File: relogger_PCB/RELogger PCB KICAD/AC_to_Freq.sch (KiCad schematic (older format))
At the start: 4 parts, among them IC2 FOD817ASD

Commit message: Update of schematic
By ML
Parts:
- IC2: value FOD817ASD -> VO615A; Description (none) -> Opto-coupler; Manufacturer (none) -> Vishay; Manufacturer Part No (none) -> VO615A-5; Supplier 1 (none) -> RS; Supplier 1 Cost (none) -> 0.12; Supplier 1 Part No (none) -> 773-3693
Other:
- moved on the sheet: D15, IC2, R19, R20
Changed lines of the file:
@@
 LIBS:matts_components
 LIBS:linear2
-LIBS:ds3231
-LIBS:micro_sd
 LIBS:RELogger_PCB_v1-cache
 EELAYER 25 0
@@
 Comment4 ""
 $EndDescr
-Text HLabel 6600 2150 2    60   Input ~ 0
+Text HLabel 7600 4100 2    60   Input ~ 0
 GND
-Text HLabel 3250 1300 0    60   Input ~ 0
+Text HLabel 4250 3250 0    60   Input ~ 0
 AC_IN+
-Text HLabel 6650 1950 2    60   Output ~ 0
+Text HLabel 7650 3900 2    60   Output ~ 0
 Freq_OUT
-Text HLabel 3300 2350 0    60   Input ~ 0
+Text HLabel 4300 4300 0    60   Input ~ 0
 AC_IN-
 $Comp
 L FOD817ASD IC2
 U 1 1 57B10CC2
-P 4300 2050
-F 0 "IC2" H 4112 2227 40  0000 C CNN
-F 1 "FOD817ASD" H 4450 1850 40  0000 C CNN
-F 2 "" H 4650 1800 29  0000 C CNN
-F 3 "" H 4300 2050 60  0000 C CNN
-	1    4300 2050
+P 5300 4000
+F 0 "IC2" H 5112 4177 40  0000 C CNN
+F 1 "VO615A" H 5450 3800 40  0000 C CNN
+F 2 "" H 5650 3750 29  0000 C CNN
+F 3 "http://docs-europe.electrocomponents.com/webdocs/1196/0900766b81196e5a.pdf" H 5300 4000 60  0001 C CNN
+F 4 "~" H 5300 4000 60  0000 C CNN "Notes"
+F 5 "Opto-coupler" H 5300 4000 60  0001 C CNN "Description"
+F 6 "Vishay" H 5300 4000 60  0001 C CNN "Manufacturer"
+F 7 "VO615A-5" H 5300 4000 60  0001 C CNN "Manufacturer Part No"
+F 8 "RS" H 5300 4000 60  0001 C CNN "Supplier 1"
+F 9 "773-3693" H 5300 4000 60  0001 C CNN "Supplier 1 Part No"
+F 10 "0.12" H 5300 4000 60  0001 C CNN "Supplier 1 Cost"
+F 11 "~" H 5300 4000 60  0001 C CNN "Supplier 2"
+F 12 "~" H 5300 4000 60  0001 C CNN "Supplier 2 Part No"
+F 13 "~" H 5300 4000 60  0001 C CNN "Supplier 2 Cost"
+	1    5300 4000
 	1    0    0    -1
 $EndComp
@@
 L R R19
 U 1 1 57B10D47
-P 3800 1700
-F 0 "R19" V 3880 1700 50  0000 C CNN
-F 1 "1k" V 3800 1700 50  0000 C CNN
-F 2 "" V 3730 1700 50  0000 C CNN
-F 3 "" H 3800 1700 50  0000 C CNN
-F 4 "~" H 3800 1700 60  0001 C CNN "Description"
-F 5 "~" H 3800 1700 60  0001 C CNN "Notes"
-F 6 "~" H 3800 1700 60  0001 C CNN "Manufacturer"
-F 7 "~" H 3800 1700 60  0001 C CNN "Manufacturer Part No"
-F 8 "~" H 3800 1700 60  0001 C CNN "Supplier 1"
-F 9 "~" H 3800 1700 60  0001 C CNN "Supplier 1 Part No"
-F 10 "~" H 3800 1700 60  0001 C CNN "Supplier 2"
-F 11 "~" H 3800 1700 60  0001 C CNN "Supplier 2 Part No"
-F 12 "~" H 3800 1700 60  0001 C CNN "Cost"
-	1    3800 1700
+P 4800 3650
+F 0 "R19" V 4880 3650 50  0000 C CNN
+F 1 "1k" V 4800 3650 50  0000 C CNN
+F 2 "" V 4730 3650 50  0000 C CNN
+F 3 "" H 4800 3650 50  0000 C CNN
+F 4 "~" H 4800 3650 60  0001 C CNN "Description"
+F 5 "~" H 4800 3650 60  0001 C CNN "Notes"
+F 6 "~" H 4800 3650 60  0001 C CNN "Manufacturer"
+F 7 "~" H 4800 3650 60  0001 C CNN "Manufacturer Part No"
+F 8 "~" H 4800 3650 60  0001 C CNN "Supplier 1"
+F 9 "~" H 4800 3650 60  0001 C CNN "Supplier 1 Part No"
+F 10 "~" H 4800 3650 60  0001 C CNN "Supplier 2"
+F 11 "~" H 4800 3650 60  0001 C CNN "Supplier 2 Part No"
+F 12 "~" H 4800 3650 60  0001 C CNN "Cost"
+	1    4800 3650
 	1    0    0    -1
 $EndComp
 Wire Wire Line
-	3800 1300 3800 1550
+	4800 3250 4800 3500
 Wire Wire Line
-	3950 1950 3800 1950
+	4950 3900 4800 3900
 Wire Wire Line
-	3800 1950 3800 1850
+	4800 3900 4800 3800
 Wire Wire Line
-	3950 2150 3800 2150
+	4950 4100 4800 4100
 Wire Wire Line
-	3800 2150 3800 2350
+	4800 4100 4800 4300
 Wire Wire Line
-	3800 2350 3300 2350
+	4800 4300 4300 4300
 $Comp
 L D D15
 U 1 1 57B11038
-P 3500 1300
-F 0 "D15" H 3500 1400 50  0000 C CNN
-F 1 "1N4001" H 3500 1200 50  0000 C CNN
-F 2 "" H 3500 1300 50  0000 C CNN
-F 3 "" H 3500 1300 50  0000 C CNN
-	1    3500 1300
+P 4500 3250
+F 0 "D15" H 4500 3350 50  0000 C CNN
+F 1 "1N4001" H 4500 3150 50  0000 C CNN
+F 2 "" H 4500 3250 50  0000 C CNN
+F 3 "" H 4500 3250 50  0000 C CNN
+	1    4500 3250
 	-1   0    0    1
 $EndComp
 Wire Wire Line
-	3650 1300 3800 1300
+	4650 3250 4800 3250
 Wire Wire Line
-	3350 1300 3250 1300
-Text HLabel 6600 1350 2    60   Output ~ 0
+	4350 3250 4250 3250
+Text HLabel 7600 3300 2    60   Output ~ 0
 Vss
 $Comp
 L R R20
 U 1 1 57B1112A
-P 4950 1550
-F 0 "R20" V 5030 1550 50  0000 C CNN
-F 1 "10k" V 4950 1550 50  0000 C CNN
-F 2 "" V 4880 1550 50  0000 C CNN
-F 3 "" H 4950 1550 50  0000 C CNN
-	1    4950 1550
+P 5950 3500
+F 0 "R20" V 6030 3500 50  0000 C CNN
+F 1 "10k" V 5950 3500 50  0000 C CNN
+F 2 "" V 5880 3500 50  0000 C CNN
+F 3 "" H 5950 3500 50  0000 C CNN
+	1    5950 3500
 	1    0    0    -1
 $EndComp
 Wire Wire Line
-	6600 1350 4950 1350
+	7600 3300 5950 3300
 Wire Wire Line
-	4950 1350 4950 1400
+	5950 3300 5950 3350
 Wire Wire Line
-	4650 1950 6650 1950
+	5650 3900 7650 3900
 Wire Wire Line
-	4950 1950 4950 1700
+	5950 3900 5950 3650
 Wire Wire Line
-	4650 2150 6600 2150
-Connection ~ 4950 1950
+	5650 4100 7600 4100
+Connection ~ 5950 3900
 $EndSCHEMATC

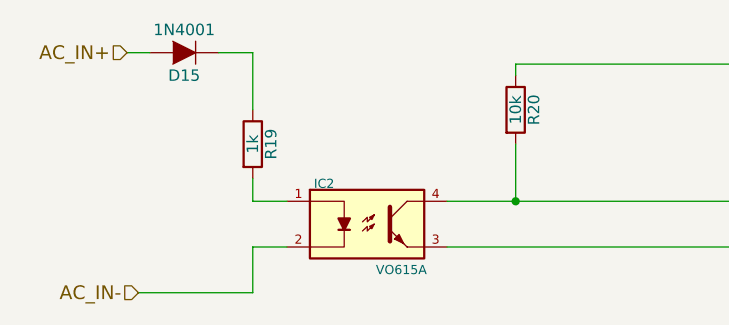
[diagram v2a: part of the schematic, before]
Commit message: Schematic update and PCB initial run
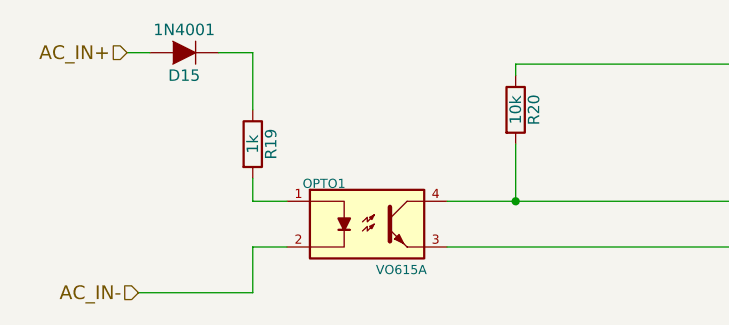
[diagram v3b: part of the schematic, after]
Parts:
- D15: footprint (none) -> REInnovationFootprint:TH_Diode_1
- OPTO1: renamed from IC2; footprint (none) -> REInnovationFootprint:DIP-4_300_ELL
- R19, R20: footprint (none) -> REInnovationFootprint:TH_Resistor_1
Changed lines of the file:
@@
 AC_IN-
 $Comp
-L FOD817ASD IC2
+L FOD817ASD OPTO1
 U 1 1 57B10CC2
 P 5300 4000
-F 0 "IC2" H 5112 4177 40  0000 C CNN
+F 0 "OPTO1" H 5112 4177 40  0000 C CNN
 F 1 "VO615A" H 5450 3800 40  0000 C CNN
-F 2 "" H 5650 3750 29  0000 C CNN
+F 2 "REInnovationFootprint:DIP-4_300_ELL" H 5650 3750 29  0001 C CNN
 F 3 "http://docs-europe.electrocomponents.com/webdocs/1196/0900766b81196e5a.pdf" H 5300 4000 60  0001 C CNN
 F 4 "~" H 5300 4000 60  0000 C CNN "Notes"
@@
 F 0 "R19" V 4880 3650 50  0000 C CNN
 F 1 "1k" V 4800 3650 50  0000 C CNN
-F 2 "" V 4730 3650 50  0000 C CNN
+F 2 "REInnovationFootprint:TH_Resistor_1" V 4730 3650 50  0001 C CNN
 F 3 "" H 4800 3650 50  0000 C CNN
 F 4 "~" H 4800 3650 60  0001 C CNN "Description"
@@
 F 0 "D15" H 4500 3350 50  0000 C CNN
 F 1 "1N4001" H 4500 3150 50  0000 C CNN
-F 2 "" H 4500 3250 50  0000 C CNN
+F 2 "REInnovationFootprint:TH_Diode_1" H 4500 3250 50  0001 C CNN
 F 3 "" H 4500 3250 50  0000 C CNN
 	1    4500 3250
@@
 F 0 "R20" V 6030 3500 50  0000 C CNN
 F 1 "10k" V 5950 3500 50  0000 C CNN
-F 2 "" V 5880 3500 50  0000 C CNN
+F 2 "REInnovationFootprint:TH_Resistor_1" V 5880 3500 50  0001 C CNN
 F 3 "" H 5950 3500 50  0000 C CNN
 	1    5950 3500
